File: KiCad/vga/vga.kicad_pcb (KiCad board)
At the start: 4 copper layers, 199.9 x 120.4 mm, 57 parts, among them J1 DB15_Female_HighDensity_Mount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, U1 EPM7128S, U10 74HC245, U11 74HC245, U12 74AC573, U13 74AC573, U14 EPM7064S, U15 74AC573, U16 74AC573, U17 74AC245, U18 27C512, U19 74AC151, U2 61256-15, U3 61256-15, U4 61256-15, U5 61256-15, U6 74HC245, U7 74HC245, U8 74HC245, U9 74HC245, X1 50 MHz, X2 Edge72

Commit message: Updated KiCad VGA board and main board.
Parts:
- added U20: 74HC04, Package_SO:SO-14_5.3x10.2mm_P1.27mm, F.Cu at (82.0, 93.3)
- R10, R11: value 100 -> 47
- R9: value 100 -> 56
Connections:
- net M_~IO renamed Net-(X2-Pad65)
- U1 pad 23: ~CS_R3 -> Net-(U1-Pad23)
- U1 pad 24: CPU_RAM_DIR -> ~CS_R3
- U1 pad 41: Net-(U1-Pad41) -> ~CHAR_BG
- U1 pad 48: Net-(U1-Pad48) -> ~CHR_TO_COL
- U1 pad 49: ~CHAR_BG -> ~CPU_RAM0
- U1 pad 5: Net-(U1-Pad5) -> IRQ5
- U1 pad 50: ~CHR_TO_COL -> ~CPU_RAM1
- U1 pad 51: ~CPU_RAM0 -> ~CPU_RAM2
- U1 pad 52: ~CPU_RAM1 -> ~CPU_RAM3
- U1 pad 54: ~CPU_RAM2 -> CPU_RAM_DIR
- U1 pad 55: ~CPU_RAM3 -> RA14
- U1 pad 56: Net-(U1-Pad56) -> RA13
- U1 pad 57: RA14 -> RA12
- U1 pad 58: RA13 -> RA11
- U1 pad 6: A0 -> Net-(U1-Pad6)
- U1 pad 60: RA12 -> RA10
- U1 pad 61: RA11 -> RA9
- U1 pad 62: RA10 -> Net-(U1-Pad62)
- U1 pad 63: RA9 -> RA8
- U1 pad 64: RA8 -> RA7
- U1 pad 65: RA7 -> RA6
- U1 pad 67: RA6 -> RA5
- U1 pad 68: RA5 -> RA4
- U1 pad 69: RA4 -> RA3
- U1 pad 70: RA3 -> RA2
- U1 pad 71: RA2 -> Net-(U1-Pad71)
- U1 pad 8: A1 -> A0
- U1 pad 81: Net-(U1-Pad81) -> /CPLD/EN_IRQ
- U1 pad 9: A2 -> A1
- U14 pad 11: D4 -> D5
- U14 pad 12: D3 -> D4
- U14 pad 13: D2 -> Net-(U14-Pad13)
- U14 pad 14: D1 -> D3
- U14 pad 16: D0 -> D2
- U14 pad 17: ~VGA_IO -> D1
- U14 pad 18: ~WR -> D0
- U14 pad 37: Net-(U14-Pad37) -> ~WR
- U14 pad 39: Net-(U14-Pad39) -> ~VGA_IO
- U14 pad 40: Net-(U14-Pad40) -> /CPLD/EN_IRQ
- U14 pad 7: D7 -> Net-(U14-Pad7)
- U14 pad 8: D6 -> D7
- U14 pad 9: D5 -> D6
- X2 pad 60: Net-(X2-Pad60) -> IRQ5
- X2 pad 69: RESET -> Net-(U20-Pad1)
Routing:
- net ~WR: track 175.6 -> 49.0 mm, vias 4 -> 2
- net ~CHR_TO_COL: track 0.00 -> 111.2 mm, vias 0 -> 1
- net A1: track 109.4 -> 0.00 mm, vias 1 -> 0
- net CHROW1: track 0.00 -> 81.5 mm, vias 0 -> 1
- net CHROW0: track 0.00 -> 81.0 mm, vias 0 -> 1
- net CHROW3: track 0.00 -> 80.9 mm, vias 0 -> 1
- net CHROW2: track 0.00 -> 79.4 mm, vias 0 -> 1
- net RA13: track 60.2 -> 116.6 mm, vias 0 -> 1
- net RA14: track 60.3 -> 108.2 mm, vias 0 -> 1
- net RA10: track 59.9 -> 106.0 mm, vias 0 -> 1
- net R1D2: track 37.8 -> 79.5 mm, vias 0 -> 2
- net R2D2: track 37.1 -> 78.1 mm, vias 0 -> 2
- net RA9: track 99.1 -> 140.1 mm, vias 0 -> 1
- net R0D2: track 38.1 -> 78.3 mm, vias 0 -> 2
- net R2D1: track 37.1 -> 77.2 mm, vias 0 -> 2
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- added copper zone on B.Cu, net GND
- added copper zone on F.Cu, net GND
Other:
- outline, holes or cut-outs redrawn
- board text added: "128 K RAM"

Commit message: Updated graphics adapter
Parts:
- added R12: 4K7, Resistor_THT:R_Axial_DIN0204_L3.6mm_D1.6mm_P7.62mm_Horizontal, F.Cu at (125.7, 69.5)
- C17: footprint Capacitor_THT:C_Disc_D3.4mm_W2.1mm_P2.50mm -> Capacitor_THT:C_Disc_D4.3mm_W1.9mm_P5.00mm
- J1: value DB15_Female_HighDensity_MountingHoles -> VGA connector
- U17: value 74AC245 -> 74HC245
- U19: value 74AC151 -> 74AC166
- U20: value 74HC04 -> 74HC00; footprint Package_SO:SO-14_5.3x10.2mm_P1.27mm -> Package_DIP:DIP-14_W7.62mm_LongPads
- moved U20 12.0 mm to (71.4, 98.8), turned to 90 degrees
- moved U19 1.02 mm to (87.9, 128.3)
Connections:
- J1 pad 13: ~H_SYNC -> HSYNC
- J1 pad 14: ~V_SYNC -> VSYNC
- U1 pad 27: LATCH -> PX_CLK
- U1 pad 44: CHCOL0 -> LATCH_CHR
- U1 pad 45: CHCOL1 -> LATCH_COL
- U1 pad 46: CHCOL2 -> ~PE_CHPX
- U1 pad 5: IRQ5 -> Net-(U1-Pad5)
- U1 pad 75: ~H_SYNC -> HSYNC
- U1 pad 76: ~V_SYNC -> VSYNC
- U1 pad 81: /CPLD/EN_IRQ -> Net-(U1-Pad81)
- U11 pad 9: GND -> Net-(R12-Pad1)
- U12 pad 11: LATCH -> LATCH_CHR
- U13 pad 11: LATCH -> LATCH_COL
- U14 pad 2: ~CHAR_BG -> Net-(U14-Pad2)
- U14 pad 29: Net-(U14-Pad29) -> A1
- U14 pad 3: A1 -> VCC
- U14 pad 31: Net-(U14-Pad31) -> A0
- U14 pad 33: Net-(U14-Pad33) -> HSYNC
- U14 pad 34: Net-(U14-Pad34) -> VSYNC
- U14 pad 4: A2 -> ~CHAR_BG
- U14 pad 40: /CPLD/EN_IRQ -> IRQ5
- U14 pad 43: Net-(U1-Pad83) -> PCLK
- U14 pad 5: /CPLD/MODE1 -> /CPLD/MODE0
- U14 pad 6: /CPLD/MODE0 -> /CPLD/MODE1
- U15 pad 11: LATCH -> LATCH_CHR
- U16 pad 11: LATCH -> LATCH_COL
- U19 pad 1: Net-(U18-Pad15) -> GND
- U19 pad 10: CHCOL1 -> Net-(U18-Pad16)
- U19 pad 11: CHCOL0 -> Net-(U18-Pad17)
- U19 pad 12: Net-(U18-Pad19) -> Net-(U18-Pad18)
- U19 pad 13: Net-(U18-Pad18) -> ~CHARPIXEL
- U19 pad 14: Net-(U18-Pad17) -> Net-(U18-Pad19)
- U19 pad 15: Net-(U18-Pad16) -> ~PE_CHPX
- U19 pad 2: Net-(U18-Pad13) -> Net-(U18-Pad11)
- U19 pad 4: Net-(U18-Pad11) -> Net-(U18-Pad13)
- U19 pad 5: Net-(U19-Pad5) -> Net-(U18-Pad15)
- U19 pad 6: ~CHARPIXEL -> ~CHARMODE
- U19 pad 7: ~CHARMODE -> PX_CLK
- U19 pad 9: CHCOL2 -> VCC
- U20 pad 1: Net-(U20-Pad1) -> /connector/RESET
- U20 pad 10: Net-(U20-Pad10) -> GND
- U20 pad 11: GND -> Net-(U20-Pad11)
- U20 pad 12: Net-(U20-Pad12) -> GND
- U20 pad 14: (no net) -> VCC
- U20 pad 2: ~RESET -> /connector/RESET
- U20 pad 3: GND -> ~RESET
- U20 pad 4: Net-(U20-Pad4) -> GND
- U20 pad 7: (no net) -> GND
- X2 pad 30: Net-(X2-Pad30) -> PCLK
- X2 pad 69: Net-(U20-Pad1) -> /connector/RESET
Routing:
- net LATCH: track 247.3 -> 0.00 mm, vias 2 -> 0
- net A1: track 0.00 -> 205.8 mm, vias 0 -> 3
- net ~V_SYNC: track 193.9 -> 0.00 mm, vias 1 -> 0
- net VSYNC: track 0.00 -> 193.9 mm, vias 0 -> 1
- net ~H_SYNC: track 190.9 -> 0.00 mm
- net HSYNC: track 0.00 -> 190.9 mm
- net ~CS_R3: track 0.00 -> 173.8 mm, vias 0 -> 1
- net D12: track 39.0 -> 204.0 mm, vias 0 -> 1
- net D11: track 39.3 -> 201.2 mm, vias 0 -> 1
- net D10: track 39.0 -> 198.7 mm, vias 0 -> 1
- net PCLK: track 0.00 -> 157.5 mm, vias 0 -> 3
- net D9: track 39.0 -> 196.0 mm, vias 0 -> 1
- net D8: track 39.3 -> 195.4 mm, vias 0 -> 1
- net ~CS_R2: track 0.00 -> 155.9 mm, vias 0 -> 1
- net ~CPU_RAM3: track 0.00 -> 154.5 mm, vias 0 -> 1
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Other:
- board text added: "Mini8086 VGA adapter"
- board text added: "Rev 1.0 2020"
- board text removed: "Mini8086 VGA adapter 1.0"
- board text removed: "SP 2020"

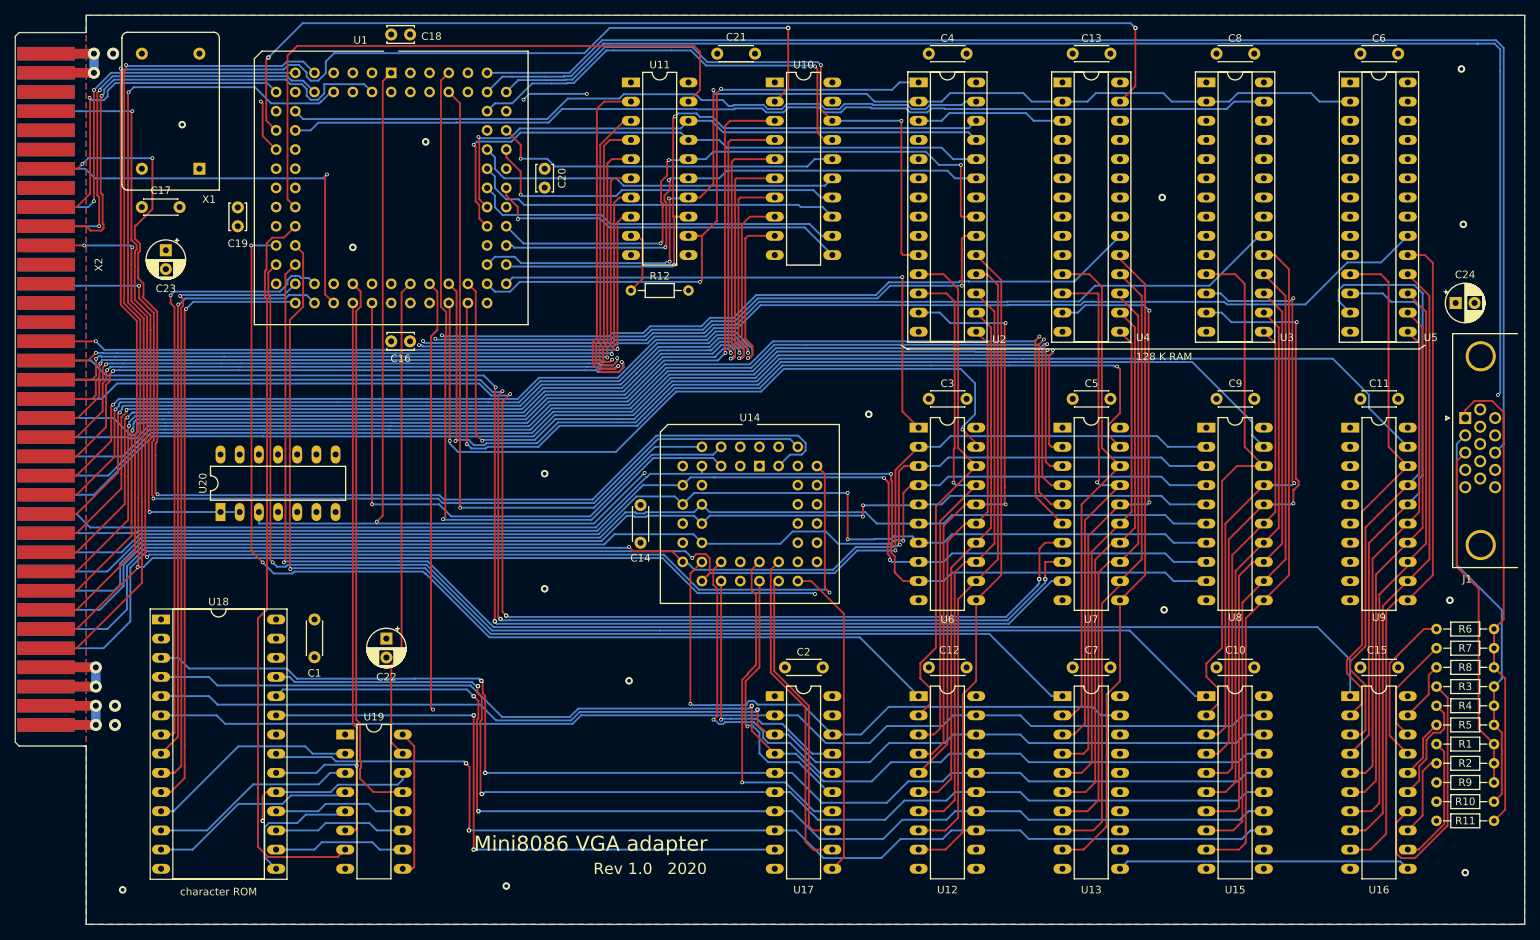
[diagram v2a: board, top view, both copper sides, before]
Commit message: Replaced MAX7000 CPLD with MAX II in graphics adapter. PCB redesign with smaller size.
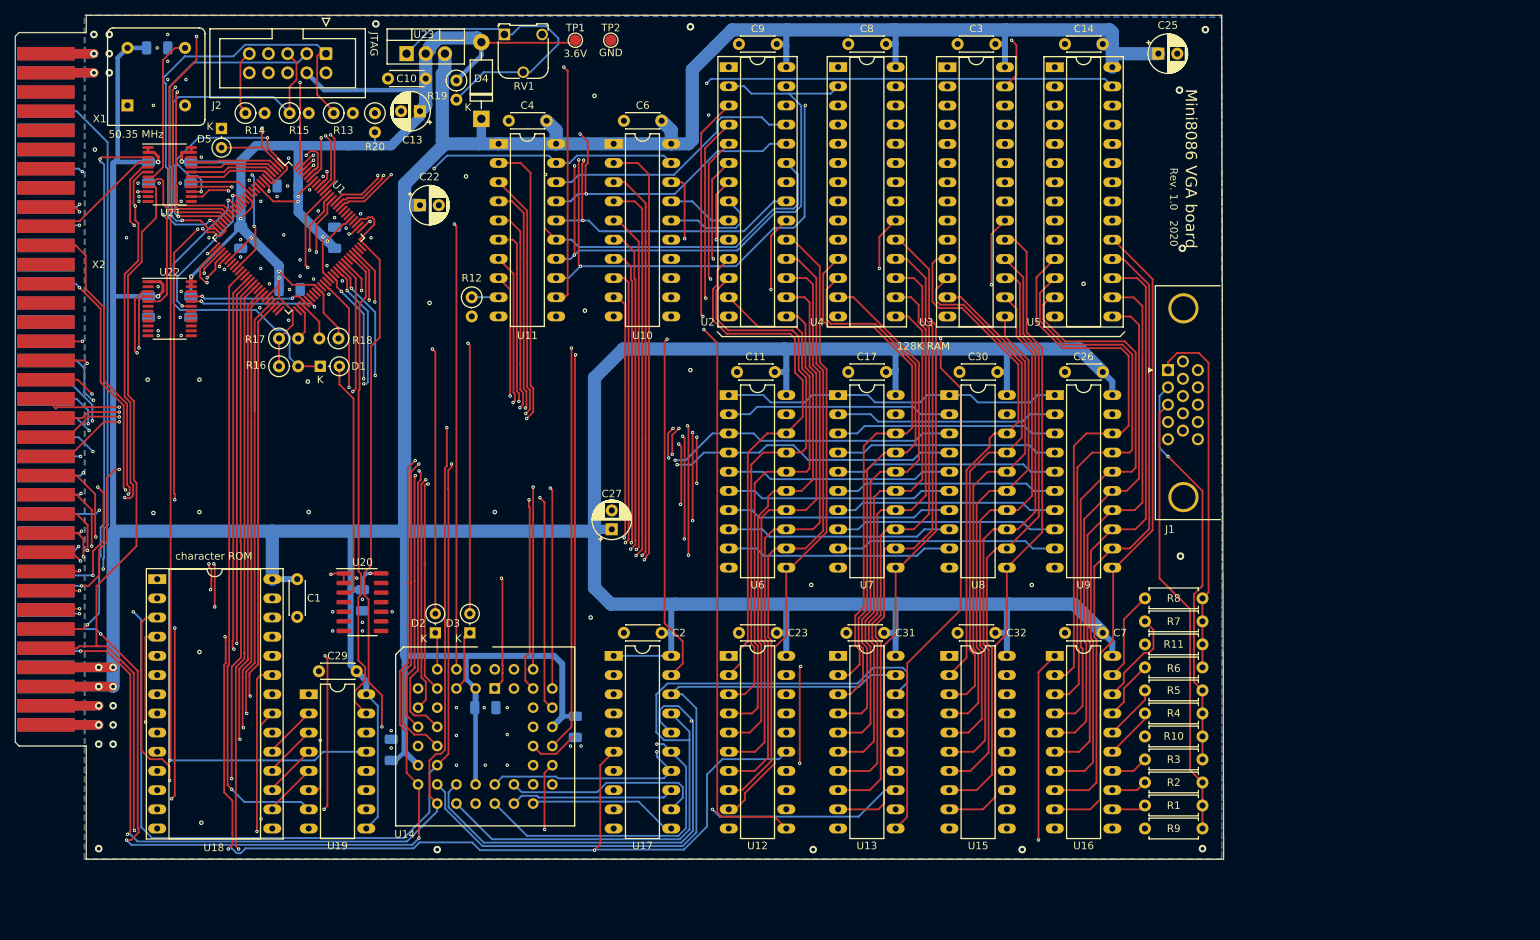
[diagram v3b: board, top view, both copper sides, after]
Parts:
- added C25: 10µ, Capacitor_THT:CP_Radial_D5.0mm_P2.50mm, F.Cu at (195.6, 38.1)
- added C26: 100n, Capacitor_THT:C_Disc_D4.3mm_W1.9mm_P5.00mm, F.Cu at (188.2, 80.3)
- added C27: 10µ, Capacitor_THT:CP_Radial_D5.0mm_P2.50mm, F.Cu at (123.2, 101.1)
- added C28: 100n, Capacitor_SMD:C_1206_3216Metric, B.Cu at (118.4, 127.3)
- added C29: 100n, Capacitor_THT:C_Disc_D4.3mm_W1.9mm_P5.00mm, F.Cu at (89.4, 119.9)
- added C30: 100n, Capacitor_THT:C_Disc_D4.3mm_W1.9mm_P5.00mm, F.Cu at (174.2, 80.3)
- added C31: 100n, Capacitor_THT:C_Disc_D4.3mm_W1.9mm_P5.00mm, F.Cu at (159.3, 114.8)
- added C32: 100n, Capacitor_THT:C_Disc_D4.3mm_W1.9mm_P5.00mm, F.Cu at (174.0, 114.8)
- added C33: 100n, Capacitor_SMD:C_1206_3216Metric, B.Cu at (80.5, 69.3)
- added C34: 100n, Capacitor_SMD:C_1206_3216Metric, B.Cu at (86.5, 62.5)
- added C35: 100n, Capacitor_SMD:C_1206_3216Metric, B.Cu at (94.0, 130.3)
- added D1: BAT43, Diode_THT:D_DO-34_SOD68_P2.54mm_Vertical_KathodeUp, F.Cu at (84.6, 79.5)
- added D2: BAT43, Diode_THT:D_DO-34_SOD68_P2.54mm_Vertical_KathodeUp, F.Cu at (99.8, 114.8)
- added D3: BAT43, Diode_THT:D_DO-34_SOD68_P2.54mm_Vertical_KathodeUp, F.Cu at (104.4, 114.8)
- added D4: 1N4001, Diode_THT:D_DO-41_SOD81_P10.16mm_Horizontal, F.Cu at (105.9, 46.7)
- added D5: BAT43, Diode_THT:D_DO-34_SOD68_P2.54mm_Vertical_KathodeUp, F.Cu at (71.5, 48.0)
- added J2: JTAG, Connector_IDC:IDC-Header_2x05_P2.54mm_Vertical, F.Cu at (85.3, 38.1)
- added R13: 1K, Resistor_THT:R_Axial_DIN0207_L6.3mm_D2.5mm_P2.54mm_Vertical, F.Cu at (86.4, 46.0)
- added R14: 10K, Resistor_THT:R_Axial_DIN0207_L6.3mm_D2.5mm_P2.54mm_Vertical, F.Cu at (74.7, 46.0)
- added R15: 10K, Resistor_THT:R_Axial_DIN0207_L6.3mm_D2.5mm_P2.54mm_Vertical, F.Cu at (80.5, 46.0)
- added R16: 1K, Resistor_THT:R_Axial_DIN0207_L6.3mm_D2.5mm_P2.54mm_Vertical, F.Cu at (79.1, 79.5)
- added R17: 1K, Resistor_THT:R_Axial_DIN0207_L6.3mm_D2.5mm_P2.54mm_Vertical, F.Cu at (79.1, 75.8)
- added R18: 1K, Resistor_THT:R_Axial_DIN0207_L6.3mm_D2.5mm_P2.54mm_Vertical, F.Cu at (87.0, 75.8)
- added R19: 220, Resistor_THT:R_Axial_DIN0207_L6.3mm_D2.5mm_P2.54mm_Vertical, F.Cu at (102.6, 41.7)
- added R20: 1K, Resistor_THT:R_Axial_DIN0207_L6.3mm_D2.5mm_P2.54mm_Vertical, F.Cu at (91.8, 46.0)
- added RV1: 500, Potentiometer_THT:Potentiometer_Runtron_RM-065_Vertical, F.Cu at (109.0, 35.6)
- added TP1: 3.6V, TestPoint:TestPoint_Pad_D1.5mm, F.Cu at (118.4, 36.3)
- added TP2: GND, TestPoint:TestPoint_Pad_D1.5mm, F.Cu at (123.1, 36.3)
- added U21: 74LVC4245A, Package_SO:TSSOP-24_4.4x7.8mm_P0.65mm, F.Cu at (64.6, 54.1)
- added U22: 74LVC4245A, Package_SO:TSSOP-24_4.4x7.8mm_P0.65mm, F.Cu at (64.6, 71.9)
- added U23: LM317_TO-220, Package_TO_SOT_THT:TO-220-3_Vertical, F.Cu at (96.0, 38.1)
- C12, C15, C21, C5: footprint Capacitor_THT:C_Disc_D4.3mm_W1.9mm_P5.00mm -> Capacitor_SMD:C_1206_3216Metric; moved to B.Cu
- C13: value 100n -> 10µ; footprint Capacitor_THT:C_Disc_D4.3mm_W1.9mm_P5.00mm -> Capacitor_THT:CP_Radial_D5.0mm_P2.50mm
- C16, C18, C19, C20: footprint Capacitor_THT:C_Disc_D3.4mm_W2.1mm_P2.50mm -> Capacitor_SMD:C_1206_3216Metric; moved to B.Cu
- C22: value 10µ -> 47µ
- C23: value 10µ -> 100n; footprint Capacitor_THT:CP_Radial_D5.0mm_P2.50mm -> Capacitor_THT:C_Disc_D4.3mm_W1.9mm_P5.00mm
- C24: value 10µ -> 100n; footprint Capacitor_THT:CP_Radial_D5.0mm_P2.50mm -> Capacitor_SMD:C_1206_3216Metric; moved to B.Cu
- R1, R10, R11, R2, R3, R4, R5, R6, R7, R8, R9: footprint Resistor_THT:R_Axial_DIN0204_L3.6mm_D1.6mm_P7.62mm_Horizontal -> Resistor_THT:R_Axial_DIN0207_L6.3mm_D2.5mm_P7.62mm_Horizontal
- R12: footprint Resistor_THT:R_Axial_DIN0204_L3.6mm_D1.6mm_P7.62mm_Horizontal -> Resistor_THT:R_Axial_DIN0207_L6.3mm_D2.5mm_P2.54mm_Vertical
- U1: value EPM7128S -> EPM240T100; footprint Package_LCC:PLCC-84_THT-Socket -> Package_QFP:LQFP-100_14x14mm_P0.5mm
- U17: value 74HC245 -> 74AC245
- U19: value 74AC166 -> 74F166
- U20: footprint Package_DIP:DIP-14_W7.62mm_LongPads -> Package_SO:SOIC-14_3.9x8.7mm_P1.27mm
- X1: value 50 MHz -> 50.35 MHz; footprint Oscillator:Oscillator_DIP-14 -> Oscillator:Oscillator_DIP-8
- moved C15 183.7 mm to (63.0, 37.3), turned to 0 degrees
- moved C24 168.4 mm to (67.4, 53.8), turned to 270 degrees
- moved C10 134.6 mm to (98.6, 41.4)
- moved C12 126.6 mm to (61.8, 53.8), turned to 270 degrees
- moved C5 102.6 mm to (90.2, 110.5), turned to 270 degrees
- moved C17 100.9 mm to (159.5, 80.3), turned to 180 degrees
- moved C6 97.9 mm to (129.8, 47.0)
- moved C23 95.5 mm to (145.0, 114.8), turned to 180 degrees
- moved C13 91.8 mm to (97.8, 45.7)
- moved C14 90.0 mm to (188.2, 36.8), turned to 180 degrees
- moved C11 82.6 mm to (144.8, 80.3)
- moved C9 78.8 mm to (145.0, 36.8)
- moved C21 77.4 mm to (67.4, 71.6), turned to 270 degrees
- moved C20 71.8 mm to (106.4, 124.7), turned to 0 degrees
- moved C22 57.6 mm to (97.8, 58.2), turned to 0 degrees
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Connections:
- C10 pad 1: VCC -> VCC36
- C13 pad 1: VCC -> VCC36
- C16 pad 1: VCC -> VCC36
- C19 pad 1: VCC -> VCC36
- C21 pad 1: VCC -> VCC36
- C24 pad 1: VCC -> VCC36
- U1 pad 1: ~RESET -> /CPLD/PLANE
- U1 pad 10: ~RD -> GND
- U1 pad 11: ~WR -> GND
- U1 pad 12: RDY1 -> /CPLD/CPLD_CLK_3
- U1 pad 13: VCC -> VCC36
- U1 pad 15: ~WE_R0 -> RDY1_3
- U1 pad 16: ~WE_R1 -> Net-(U1-Pad16)
- U1 pad 17: ~WE_R2 -> /CPLD/~RESET_3
- U1 pad 18: ~WE_R3 -> Net-(U1-Pad18)
- U1 pad 19: GND -> ~WE_R0
- U1 pad 2: Net-(U1-Pad2) -> /CPLD/A1_3
- U1 pad 20: ~CS_R0 -> ~WE_R1
- U1 pad 21: ~CS_R1 -> ~WE_R2
- U1 pad 22: ~CS_R2 -> Net-(J2-Pad5)
- U1 pad 24: ~CS_R3 -> Net-(J2-Pad1)
- U1 pad 25: ~CPU_RAM_ADDR -> Net-(J2-Pad3)
- U1 pad 26: VCC -> ~WE_R3
- U1 pad 27: PX_CLK -> ~CS_R0
- U1 pad 28: ~OE_L0 -> ~CS_R1
- U1 pad 29: ~OE_L1 -> ~CS_R2
- U1 pad 3: VCC -> /CPLD/~VGA_MEM_3
- U1 pad 30: ~OE_L2 -> ~CS_R3
- U1 pad 31: ~OE_L3 -> VCC36
- U1 pad 33: CHROW0 -> Net-(U1-Pad33)
- U1 pad 34: CHROW1 -> ~CPU_RAM_ADDR
- U1 pad 35: CHROW2 -> Net-(U1-Pad35)
- U1 pad 36: CHROW3 -> PX_CLK
- U1 pad 37: ~BHE -> Net-(U1-Pad37)
- U1 pad 38: VCC -> ~OE_L0
- U1 pad 39: ~CHARMODE -> ~OE_L1
- U1 pad 4: ~VGA_MEM -> /CPLD/~RD_3
- U1 pad 40: ~CHARPIXEL -> ~OE_L2
- U1 pad 41: ~CHAR_BG -> ~OE_L3
- U1 pad 42: GND -> Net-(U1-Pad42)
- U1 pad 43: VCC -> CHROW0
- U1 pad 44: LATCH_CHR -> CHROW1
- U1 pad 45: LATCH_COL -> VCC36
- U1 pad 46: ~PE_CHPX -> GND
- U1 pad 47: GND -> CHROW2
- U1 pad 48: ~CHR_TO_COL -> CHROW3
- U1 pad 49: ~CPU_RAM0 -> Net-(U1-Pad49)
- U1 pad 5: Net-(U1-Pad5) -> /CPLD/~WR_3
- U1 pad 50: ~CPU_RAM1 -> Net-(U1-Pad50)
- U1 pad 51: ~CPU_RAM2 -> Net-(U1-Pad51)
- U1 pad 52: ~CPU_RAM3 -> /CPLD/MODE0_3
- U1 pad 53: VCC -> /CPLD/MODE1_3
- U1 pad 54: CPU_RAM_DIR -> /CPLD/VSYNC_3
- U1 pad 55: RA14 -> /CPLD/HSYNC_3
- U1 pad 56: RA13 -> Net-(U1-Pad56)
- U1 pad 57: RA12 -> Net-(U1-Pad57)
- U1 pad 58: RA11 -> Net-(U1-Pad58)
- U1 pad 59: GND -> VCC36
- U1 pad 6: Net-(U1-Pad6) -> /CPLD/A0_3
- U1 pad 60: RA10 -> GND
- U1 pad 61: RA9 -> CPU_RAM_DIR
- U1 pad 63: RA8 -> VCC36
- U1 pad 64: RA7 -> ~CPU_RAM3
- U1 pad 65: RA6 -> GND
- U1 pad 66: VCC -> ~CPU_RAM2
- U1 pad 67: RA5 -> ~CPU_RAM1
- U1 pad 68: RA4 -> ~CPU_RAM0
- U1 pad 69: RA3 -> ~CHR_TO_COL
- U1 pad 7: GND -> /CPLD/~BHE_3
- U1 pad 70: RA2 -> Net-(U1-Pad70)
- U1 pad 71: Net-(U1-Pad71) -> ~PE_CHPX
- U1 pad 72: GND -> LATCH_COL
- U1 pad 73: RA1 -> LATCH_CHR
- U1 pad 74: RA0 -> Net-(U1-Pad74)
- U1 pad 75: HSYNC -> Net-(U1-Pad75)
- U1 pad 76: VSYNC -> ~CHAR_BG
- U1 pad 77: /CPLD/PLANE -> CHARPIXEL_3
- U1 pad 78: VCC -> ~CHARMODE
- U1 pad 79: /CPLD/MODE0 -> GND
- U1 pad 8: A0 -> Net-(U1-Pad8)
- U1 pad 80: /CPLD/MODE1 -> VCC36
- U1 pad 82: GND -> Net-(U1-Pad82)
- U1 pad 84: Net-(U1-Pad84) -> RA0
- U1 pad 9: A1 -> VCC36
- U14 pad 41: /CPLD/PLANE -> Net-(D5-Pad1)
- U14 pad 43: PCLK -> Net-(U14-Pad43)
- U19 pad 10: Net-(U18-Pad16) -> Net-(U18-Pad15)
- U19 pad 11: Net-(U18-Pad17) -> Net-(U18-Pad13)
- U19 pad 12: Net-(U18-Pad18) -> Net-(U18-Pad12)
- U19 pad 13: ~CHARPIXEL -> CHARPIXEL
- U19 pad 14: Net-(U18-Pad19) -> Net-(U18-Pad11)
- U19 pad 2: Net-(U18-Pad11) -> Net-(U18-Pad19)
- U19 pad 3: Net-(U18-Pad12) -> Net-(U18-Pad18)
- U19 pad 4: Net-(U18-Pad13) -> Net-(U18-Pad17)
- U19 pad 5: Net-(U18-Pad15) -> Net-(U18-Pad16)
- X1 pad 8: Net-(U1-Pad83) -> VCC
- X2 pad 30: PCLK -> Net-(X2-Pad30)
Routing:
- net VCC36: track 0.00 -> 197.9 mm, vias 0 -> 10
- net PCLK: track 157.5 -> 0.00 mm, vias 3 -> 0
- net LATCH_COL: track 38.9 -> 184.0 mm, vias 0 -> 2
- net VCC: track 941.1 -> 798.3 mm, vias 2 -> 7
- net Net-(D5-Pad1): track 0.00 -> 124.5 mm, vias 0 -> 3
- net LATCH_CHR: track 38.9 -> 157.3 mm, vias 0 -> 2
- net CHARPIXEL: track 0.00 -> 106.0 mm, vias 0 -> 1
- net ~WR: track 49.0 -> 143.0 mm, vias 2 -> 4
- net /CPLD/MODE0: track 100.7 -> 8.36 mm, vias 1 -> 0
- net /CPLD/MODE1: track 91.0 -> 4.93 mm, vias 1 -> 0
- net ~CHARPIXEL: track 72.9 -> 0.00 mm
- net ~RESET: track 131.6 -> 66.6 mm
- net DCOL5: track 151.3 -> 87.0 mm
- net /CPLD/MODE0_3: track 0.00 -> 64.0 mm, vias 0 -> 1
- net D10: track 198.7 -> 135.9 mm
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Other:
- board size 199.9 x 120.4 mm -> 160 x 111.8 mm
- net class Default: via_dia 0.5 -> 0.45; via_drill 0.3 -> 0.2
- rule pad_to_mask_clearance: 0.04 -> 0.02
- rule via_min_drill: 0.3 -> 0.2
- rule via_min_size: 0.4 -> 0.45
- board text added: "128K RAM"
- board text added: "3.6V"
- board text added: "50.35 MHz"
- board text added: "GND"
- board text added: "JTAG"
- board text added: "Mini8086 VGA board"
- board text added: "Rev. 1.0 2020"
- board text removed: "128 K RAM"
- board text removed: "Mini8086 VGA adapter"
- board text removed: "Rev 1.0 2020"

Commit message: Finished VGA adapter Rev. 1.0
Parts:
- removed C21: 100n, Capacitor_SMD:C_1206_3216Metric
- added JP1: CHARPIXEL, Jumper:SolderJumper-3_P1.3mm_Open_RoundedPad1.0x1.5mm_NumberLabels, F.Cu at (60.8, 63.2)
- R13: value 1K -> 2K2
- U19: footprint Package_DIP:DIP-16_W7.62mm_LongPads -> Package_DIP:DIP-16_W7.62mm_Socket_LongPads
- U22: value 74LVC4245A -> 74ACT32; footprint Package_SO:TSSOP-24_4.4x7.8mm_P0.65mm -> Package_SO:SOIC-14_3.9x8.7mm_P1.27mm
- moved C25 149.5 mm to (59.1, 99.1)
- moved C18 4.23 mm to (64.6, 68.5)
- moved U22 1.02 mm to (64.5, 70.9)
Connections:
- net Net-(J2-Pad1) renamed /CPLD/TCK
- net Net-(J2-Pad3) renamed /CPLD/TDO
- net Net-(J2-Pad5) renamed /CPLD/TMS
- net Net-(J2-Pad9) renamed /CPLD/TDI
- D5 pad 1: Net-(D5-Pad1) -> /CPLD/PLANE
- D5 pad 2: /CPLD/PLANE -> /CPLD/PLANE_3
- R14 pad 2: GND -> VCC36
- R15 pad 2: GND -> VCC36
- R20 pad 1: /CPLD/PLANE -> /CPLD/PLANE_3
- U1 pad 1: /CPLD/PLANE -> /CPLD/PLANE_3
- U1 pad 15: RDY1_3 -> ~BLOCK_CPU
- U1 pad 17: /CPLD/~RESET_3 -> Net-(U1-Pad17)
- U1 pad 43: CHROW0 -> Net-(U1-Pad43)
- U1 pad 44: CHROW1 -> /CPLD/~RESET_3
- U1 pad 47: CHROW2 -> CHROW0
- U1 pad 48: CHROW3 -> CHROW1
- U1 pad 49: Net-(U1-Pad49) -> CHROW2
- U1 pad 50: Net-(U1-Pad50) -> CHROW3
- U1 pad 77: CHARPIXEL_3 -> /CPLD/CHARPIXEL_CPLD
- U14 pad 41: Net-(D5-Pad1) -> /CPLD/PLANE
- U22 pad 1: VCC -> /CPLD/VSYNC_3
- U22 pad 10: Net-(U22-Pad10) -> ~VGA_MEM
- U22 pad 11: GND -> Net-(U22-Pad11)
- U22 pad 14: Net-(U22-Pad14) -> VCC
- U22 pad 2: GND -> /CPLD/VSYNC_3
- U22 pad 4: HSYNC -> /CPLD/HSYNC_3
- U22 pad 5: RDY1 -> /CPLD/HSYNC_3
- U22 pad 6: Net-(U22-Pad6) -> HSYNC
- U22 pad 7: Net-(U22-Pad7) -> GND
- U22 pad 8: Net-(U22-Pad8) -> RDY1
- U22 pad 9: Net-(U22-Pad9) -> ~BLOCK_CPU
- U7 pad 19: ~CPU_RAM2 -> ~CPU_RAM1
- U8 pad 19: ~CPU_RAM1 -> ~CPU_RAM2
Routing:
- net Net-(D5-Pad1): track 124.5 -> 0.00 mm, vias 3 -> 0
- net /CPLD/PLANE: track 27.1 -> 124.0 mm, vias 1 -> 3
- net /CPLD/CHARPIXEL_CPLD: track 0.00 -> 32.4 mm, vias 0 -> 2
- net /CPLD/PLANE_3: track 0.00 -> 27.1 mm, vias 0 -> 1
- net /CPLD/~RESET_3: track 42.7 -> 16.2 mm
- net ~VGA_MEM: track 17.0 -> 42.7 mm, vias 0 -> 2
- net ~BLOCK_CPU: track 0.00 -> 22.1 mm, vias 0 -> 2
- net RDY1_3: track 20.8 -> 0.00 mm, vias 2 -> 0
- net ~CPU_RAM2: track 89.6 -> 104.4 mm
- net CHARPIXEL_3: track 25.2 -> 13.8 mm
- net ~CPU_RAM1: track 102.4 -> 92.2 mm, vias 2 -> 3
- net Net-(R19-Pad2): track 40.2 -> 30.1 mm
- net CHROW2: track 76.7 -> 67.3 mm
- net /CPLD/VSYNC_3: track 15.7 -> 23.3 mm
- net /CPLD/HSYNC_3: track 17.9 -> 24.6 mm
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- added copper zone on In1.Cu, net GND
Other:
- board text added: "EPM240T100"
- board text added: "EPM7064S"
- board text added: "JLCJLCJLCJLC"
- board text added: "U19 CMOS"
- board text added: "U19 TTL"
